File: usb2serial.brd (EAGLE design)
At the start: 12.1 x 33 mm, 16 parts, among them IC1 FT232RL

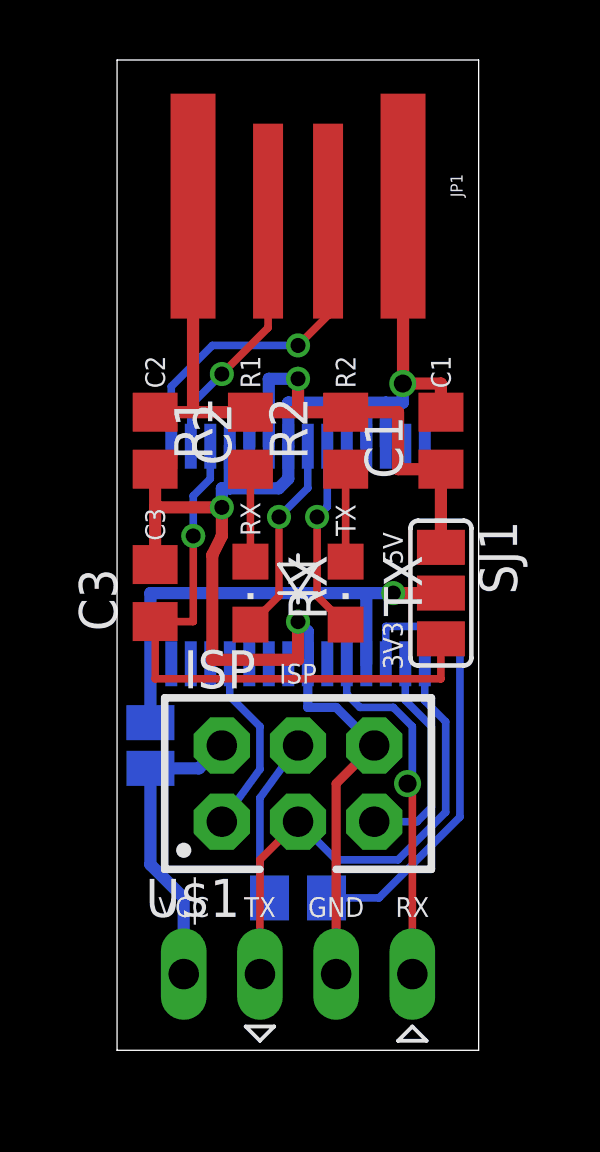
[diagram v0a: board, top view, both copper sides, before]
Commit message: Replaced the FT232R with FT230X chip
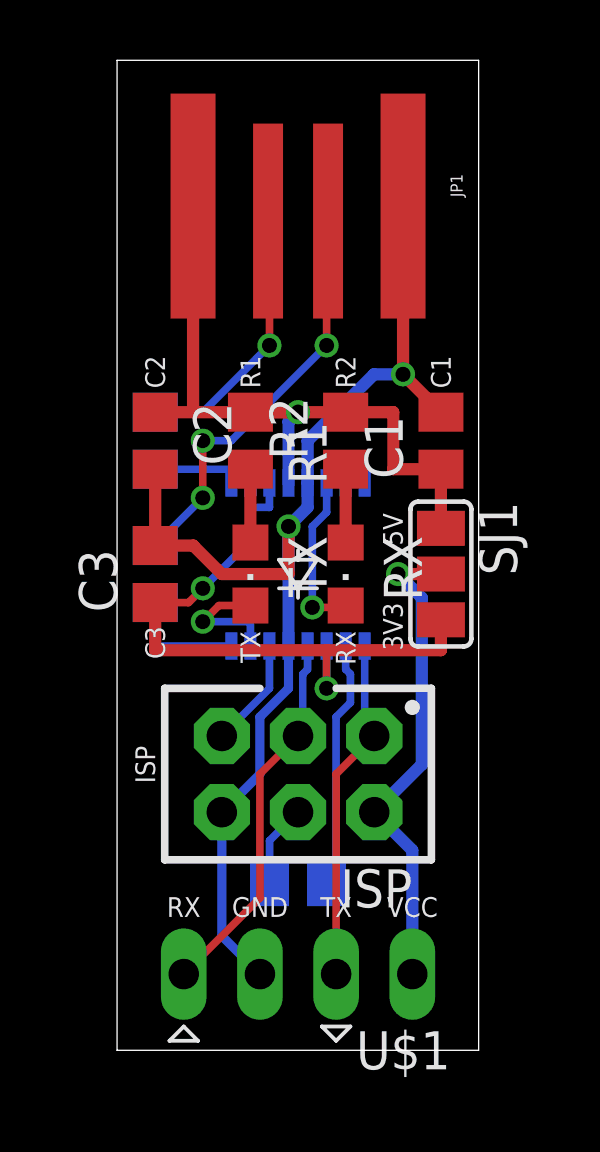
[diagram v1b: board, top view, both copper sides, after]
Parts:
- removed IC1: FT232RL, ftdichip:SSOP28
- removed SJ2: (no value), jumper:SJ
- added IC2: FT230XS, ftdichip:SSOP16
- added R3, R4: 27, rcl:R0805
- U$1: value UART-ROBOPOLY -> UART-ROBOPOLY90; device karl:929834-01-04-RK -> karl:929835-01-04-RK
- U$3: value OPEN-HARDWARE-LOGOBOTTOM -> OPEN-HARDWARE-LOGOBOTTOM-SMALL; device karl:OPEN-HARDWARE-BOTTOM -> karl:OPEN-HARDWARE-BOTTOM-SMALL
- moved U$3 4.92 mm to (6.03, 21.3)
- moved RX 3.24 mm to (7.62, 15.9)
- moved TX 3.24 mm to (4.45, 15.9)
- moved C3 0.63 mm to (1.27, 15.9)
- moved SJ1 0.63 mm to (10.8, 15.9)
- moved C4/SJ 0.48 mm to (6.03, 5.56), turned to 180 degrees
- moved ISP 0.32 mm to (6.03, 9.21), turned to 180 degrees
- turned R1 to 270 degrees
- turned U$1 to 180 degrees
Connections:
- removed net MISO: IC1.11, ISP.1
- removed net MOSI: C4/SJ.2, ISP.4
- removed net N$5: IC1.22, RX.C
- removed net N$7: R1.1, RX.A
- removed net RESET: IC1.2, ISP.5
- removed net VCCIO: IC1.4, SJ1.2, SJ2.1
- new net CTS: IC2.6, ISP.5
- new net N$2: R1.2, TX.A
- new net N$3: C4/SJ.2, IC2.2
- new net RTS: C4/SJ.1, ISP.4
- new net RXLED: IC2.14, RX.C
- new net TXLED: IC2.7, TX.C
- net 3V3: now also IC2.10, IC2.11, IC2.3; no longer IC1.17
- net GND: now also IC2.13, IC2.5; no longer IC1.18, IC1.21, IC1.25, IC1.26, IC1.7
- net N$1: now also JP1.USB_M, R4.1; no longer C4/SJ.1, IC1.3
- net N$4: now also RX.A; no longer TX.A
- net N$6: now also JP1.USB_P, R3.1; no longer IC1.23, TX.C
- net RX: now also IC2.4, ISP.3; no longer IC1.5
- net TX: now also IC2.1, ISP.1; no longer IC1.1, ISP.3
- net USBDM: now also IC2.9, R4.2; no longer IC1.16, JP1.USB_M
- net USBDP: now also IC2.8, R3.2; no longer IC1.15, JP1.USB_P
- net VCC: now also IC2.12, R1.1; no longer IC1.19, IC1.20, R1.2
- net VCCOUT: now also SJ1.2; no longer SJ2.2
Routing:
- net VCCIO: track 16.4 -> 0.00 mm, vias 1 -> 0
- net GND: track 51.0 -> 40.0 mm, vias 3 -> 2
- net N$3: track 0.00 -> 8.50 mm
- net USBDP: track 11.3 -> 3.99 mm, vias 1 -> 0
- net N$6: track 6.48 -> 13.8 mm, vias 1 -> 3
- net RESET: track 7.25 -> 0.00 mm
- net N$5: track 6.74 -> 0.00 mm, vias 1 -> 0
- net N$1: track 15.6 -> 8.92 mm, vias 0 -> 1
- net VCCOUT: track 10.0 -> 16.3 mm, vias 0 -> 1
- net MISO: track 6.09 -> 0.00 mm
- net MOSI: track 5.81 -> 0.00 mm
- net USBDM: track 8.57 -> 3.00 mm, vias 1 -> 0
- net RXLED: track 0.00 -> 5.52 mm, vias 0 -> 1
- net TX: track 16.9 -> 11.6 mm
- net TXLED: track 0.00 -> 4.21 mm, vias 0 -> 1
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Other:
- board text added: "R3"
- board text added: "R4"
- board text removed: "PWR"
- board text removed: "robopoly.ch"
